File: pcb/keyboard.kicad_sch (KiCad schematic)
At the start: 6 parts

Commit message: Modified layout further
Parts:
- added SW1: SW_Push, local-library:SW_PG1350, symbol Switch:SW_Push
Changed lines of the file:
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@@
 (kicad_sch (version 20230121) (generator eeschema)
   (paper "A4")
+  (symbol (lib_id "Switch:SW_Push") (at 59.69 83.82 0) (unit 1)
+    (in_bom yes) (on_board yes) (dnp no) (fields_autoplaced)
+    (property "Reference" "SW1" (at 59.69 77.47 0)
+      (effects (font (size 1.27 1.27)))
+    )
+    (property "Value" "SW_Push" (at 59.69 80.01 0)
+      (effects (font (size 1.27 1.27)))
+    )
+    (property "Footprint" "local-library:SW_PG1350" (at 59.69 78.74 0)
+      (effects (font (size 1.27 1.27)) hide)
+    )
+    (property "Datasheet" "~" (at 59.69 78.74 0)
+      (effects (font (size 1.27 1.27)) hide)
+    )
+    (pin "1")
+    (pin "2")
+    (instances
+      (project "keyboard"
+        (path "/fc529d87-72d0-4c92-b352-ddcf4c6f7199"
+          (reference "SW1") (unit 1)
+        )
+      )
+    )
+  )
   (symbol (lib_id "Mechanical:MountingHole") (at 20.32 119.38 0) (unit 1)
     (in_bom yes) (on_board yes) (dnp no) (fields_autoplaced)

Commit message: Working on schematic and PCB
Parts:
- removed SW1: SW_Push, local-library:SW_PG1350, symbol Switch:SW_Push
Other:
- added sheet connectors (connectors.kicad_sch)
- added sheet inputs (inputs.kicad_sch)
- added sheet power (power.kicad_sch)
- added sheet stm32 (stm32.kicad_sch)
- moved on the sheet: H1, H2, H3, H4, H5, H6
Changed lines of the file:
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@@
 (kicad_sch (version 20230121) (generator eeschema)
   (paper "A4")
-  (symbol (lib_id "Switch:SW_Push") (at 59.69 83.82 0) (unit 1)
+  (symbol (lib_id "Mechanical:MountingHole") (at 40.64 143.51 0) (unit 1)
     (in_bom yes) (on_board yes) (dnp no) (fields_autoplaced)
-    (property "Reference" "SW1" (at 59.69 77.47 0)
-      (effects (font (size 1.27 1.27)))
+    (property "Reference" "H1" (at 43.18 142.875 0)
+      (effects (font (size 1.27 1.27)) (justify left))
     )
-    (property "Value" "SW_Push" (at 59.69 80.01 0)
-      (effects (font (size 1.27 1.27)))
+    (property "Value" "MountingHole" (at 43.18 145.415 0)
+      (effects (font (size 1.27 1.27)) (justify left))
     )
-    (property "Footprint" "local-library:SW_PG1350" (at 59.69 78.74 0)
+    (property "Footprint" "MountingHole:MountingHole_3.2mm_M3" (at 40.64 143.51 0)
       (effects (font (size 1.27 1.27)) hide)
     )
-    (property "Datasheet" "~" (at 59.69 78.74 0)
-      (effects (font (size 1.27 1.27)) hide)
-    )
-    (pin "1")
-    (pin "2")
-    (instances
-      (project "keyboard"
-        (path "/fc529d87-72d0-4c92-b352-ddcf4c6f7199"
-          (reference "SW1") (unit 1)
-        )
-      )
-    )
-  )
-  (symbol (lib_id "Mechanical:MountingHole") (at 20.32 119.38 0) (unit 1)
-    (in_bom yes) (on_board yes) (dnp no) (fields_autoplaced)
-    (property "Reference" "H1" (at 22.86 118.745 0)
-      (effects (font (size 1.27 1.27)) (justify left))
-    )
-    (property "Value" "MountingHole" (at 22.86 121.285 0)
-      (effects (font (size 1.27 1.27)) (justify left))
-    )
-    (property "Footprint" "MountingHole:MountingHole_3.2mm_M3" (at 20.32 119.38 0)
-      (effects (font (size 1.27 1.27)) hide)
-    )
-    (property "Datasheet" "~" (at 20.32 119.38 0)
+    (property "Datasheet" "~" (at 40.64 143.51 0)
       (effects (font (size 1.27 1.27)) hide)
     )
@@
     )
   )
-  (symbol (lib_id "Mechanical:MountingHole") (at 20.32 129.54 0) (unit 1)
+  (symbol (lib_id "Mechanical:MountingHole") (at 60.96 143.51 0) (unit 1)
     (in_bom yes) (on_board yes) (dnp no) (fields_autoplaced)
-    (property "Reference" "H3" (at 22.86 128.905 0)
+    (property "Reference" "H3" (at 63.5 142.875 0)
       (effects (font (size 1.27 1.27)) (justify left))
     )
-    (property "Value" "MountingHole" (at 22.86 131.445 0)
+    (property "Value" "MountingHole" (at 63.5 145.415 0)
       (effects (font (size 1.27 1.27)) (justify left))
     )
-    (property "Footprint" "MountingHole:MountingHole_3.2mm_M3" (at 20.32 129.54 0)
+    (property "Footprint" "MountingHole:MountingHole_3.2mm_M3" (at 60.96 143.51 0)
       (effects (font (size 1.27 1.27)) hide)
     )
-    (property "Datasheet" "~" (at 20.32 129.54 0)
+    (property "Datasheet" "~" (at 60.96 143.51 0)
       (effects (font (size 1.27 1.27)) hide)
     )
@@
     )
   )
-  (symbol (lib_id "Mechanical:MountingHole") (at 20.32 134.62 0) (unit 1)
+  (symbol (lib_id "Mechanical:MountingHole") (at 60.96 148.59 0) (unit 1)
     (in_bom yes) (on_board yes) (dnp no) (fields_autoplaced)
-    (property "Reference" "H4" (at 22.86 133.985 0)
+    (property "Reference" "H4" (at 63.5 147.955 0)
       (effects (font (size 1.27 1.27)) (justify left))
     )
-    (property "Value" "MountingHole" (at 22.86 136.525 0)
+    (property "Value" "MountingHole" (at 63.5 150.495 0)
       (effects (font (size 1.27 1.27)) (justify left))
     )
-    (property "Footprint" "MountingHole:MountingHole_3.2mm_M3" (at 20.32 134.62 0)
+    (property "Footprint" "MountingHole:MountingHole_3.2mm_M3" (at 60.96 148.59 0)
       (effects (font (size 1.27 1.27)) hide)
     )
-    (property "Datasheet" "~" (at 20.32 134.62 0)
+    (property "Datasheet" "~" (at 60.96 148.59 0)
       (effects (font (size 1.27 1.27)) hide)
     )
@@
     )
   )
-  (symbol (lib_id "Mechanical:MountingHole") (at 20.32 139.7 0) (unit 1)
+  (symbol (lib_id "Mechanical:MountingHole") (at 81.28 143.51 0) (unit 1)
     (in_bom yes) (on_board yes) (dnp no) (fields_autoplaced)
-    (property "Reference" "H5" (at 22.86 139.065 0)
+    (property "Reference" "H5" (at 83.82 142.875 0)
       (effects (font (size 1.27 1.27)) (justify left))
     )
-    (property "Value" "MountingHole" (at 22.86 141.605 0)
+    (property "Value" "MountingHole" (at 83.82 145.415 0)
       (effects (font (size 1.27 1.27)) (justify left))
     )
-    (property "Footprint" "MountingHole:MountingHole_3.2mm_M3" (at 20.32 139.7 0)
+    (property "Footprint" "MountingHole:MountingHole_3.2mm_M3" (at 81.28 143.51 0)
       (effects (font (size 1.27 1.27)) hide)
     )
-    (property "Datasheet" "~" (at 20.32 139.7 0)
+    (property "Datasheet" "~" (at 81.28 143.51 0)
       (effects (font (size 1.27 1.27)) hide)
     )
@@
     )
   )
-  (symbol (lib_id "Mechanical:MountingHole") (at 20.32 144.78 0) (unit 1)
+  (symbol (lib_id "Mechanical:MountingHole") (at 81.28 148.59 0) (unit 1)
     (in_bom yes) (on_board yes) (dnp no) (fields_autoplaced)
-    (property "Reference" "H6" (at 22.86 144.145 0)
+    (property "Reference" "H6" (at 83.82 147.955 0)
       (effects (font (size 1.27 1.27)) (justify left))
     )
-    (property "Value" "MountingHole" (at 22.86 146.685 0)
+    (property "Value" "MountingHole" (at 83.82 150.495 0)
       (effects (font (size 1.27 1.27)) (justify left))
     )
-    (property "Footprint" "MountingHole:MountingHole_3.2mm_M3" (at 20.32 144.78 0)
+    (property "Footprint" "MountingHole:MountingHole_3.2mm_M3" (at 81.28 148.59 0)
       (effects (font (size 1.27 1.27)) hide)
     )
-    (property "Datasheet" "~" (at 20.32 144.78 0)
+    (property "Datasheet" "~" (at 81.28 148.59 0)
       (effects (font (size 1.27 1.27)) hide)
     )
@@
     )
   )
-  (symbol (lib_id "Mechanical:MountingHole") (at 20.32 124.46 0) (unit 1)
+  (symbol (lib_id "Mechanical:MountingHole") (at 40.64 148.59 0) (unit 1)
     (in_bom yes) (on_board yes) (dnp no) (fields_autoplaced)
-    (property "Reference" "H2" (at 22.86 123.825 0)
+    (property "Reference" "H2" (at 43.18 147.955 0)
       (effects (font (size 1.27 1.27)) (justify left))
     )
-    (property "Value" "MountingHole" (at 22.86 126.365 0)
+    (property "Value" "MountingHole" (at 43.18 150.495 0)
       (effects (font (size 1.27 1.27)) (justify left))
     )
-    (property "Footprint" "MountingHole:MountingHole_3.2mm_M3" (at 20.32 124.46 0)
+    (property "Footprint" "MountingHole:MountingHole_3.2mm_M3" (at 40.64 148.59 0)
       (effects (font (size 1.27 1.27)) hide)
     )
-    (property "Datasheet" "~" (at 20.32 124.46 0)
+    (property "Datasheet" "~" (at 40.64 148.59 0)
       (effects (font (size 1.27 1.27)) hide)
     )
@@
       )
     )
+  )
+  (sheet (at 38.1 88.9) (size 50.8 38.1) (fields_autoplaced)
+    (stroke (width 0.1524) (type solid))
+    (fill (color 0 0 0 0.0000))
+    (property "Sheetname" "inputs" (at 38.1 88.1884 0)
+      (effects (font (size 1.27 1.27)) (justify left bottom))
+    )
+    (property "Sheetfile" "inputs.kicad_sch" (at 38.1 127.5846 0)
+      (effects (font (size 1.27 1.27)) (justify left top))
+    )
+    (instances
+      (project "keyboard"
+        (path "/fc529d87-72d0-4c92-b352-ddcf4c6f7199" (page "4"))
+      )
+    )
+  )
+  (sheet (at 38.1 38.1) (size 50.8 38.1) (fields_autoplaced)
+    (stroke (width 0.1524) (type solid))
+    (fill (color 0 0 0 0.0000))
+    (property "Sheetname" "power" (at 38.1 37.3884 0)
+      (effects (font (size 1.27 1.27)) (justify left bottom))
+    )
+    (property "Sheetfile" "power.kicad_sch" (at 38.1 76.7846 0)
+      (effects (font (size 1.27 1.27)) (justify left top))
+    )
+    (instances
+      (project "keyboard"
+        (path "/fc529d87-72d0-4c92-b352-ddcf4c6f7199" (page "2"))
+      )
+    )
+  )
+  (sheet (at 101.6 88.9) (size 50.8 38.1) (fields_autoplaced)
+    (stroke (width 0.1524) (type solid))
+    (fill (color 0 0 0 0.0000))
+    (property "Sheetname" "stm32" (at 101.6 88.1884 0)
+      (effects (font (size 1.27 1.27)) (justify left bottom))
+    )
+    (property "Sheetfile" "stm32.kicad_sch" (at 101.6 127.5846 0)
+      (effects (font (size 1.27 1.27)) (justify left top))
+    )
+    (property "Field2" "" (at 101.6 88.9 0)
+      (effects (font (size 1.27 1.27)) hide)
+    )
+    (instances
+      (project "keyboard"
+        (path "/fc529d87-72d0-4c92-b352-ddcf4c6f7199" (page "5"))
+      )
+    )
+  )
+  (sheet (at 101.6 38.1) (size 50.8 38.1) (fields_autoplaced)
+    (stroke (width 0.1524) (type solid))
+    (fill (color 0 0 0 0.0000))
+    (property "Sheetname" "connectors" (at 101.6 37.3884 0)
+      (effects (font (size 1.27 1.27)) (justify left bottom))
+    )
+    (property "Sheetfile" "connectors.kicad_sch" (at 101.6 76.7846 0)
+      (effects (font (size 1.27 1.27)) (justify left top))
+    )
+    (property "Field2" "" (at 101.6 38.1 0)
+      (effects (font (size 1.27 1.27)) hide)
+    )
+    (instances
+      (project "keyboard"
+        (path "/fc529d87-72d0-4c92-b352-ddcf4c6f7199" (page "3"))
+      )
+    )

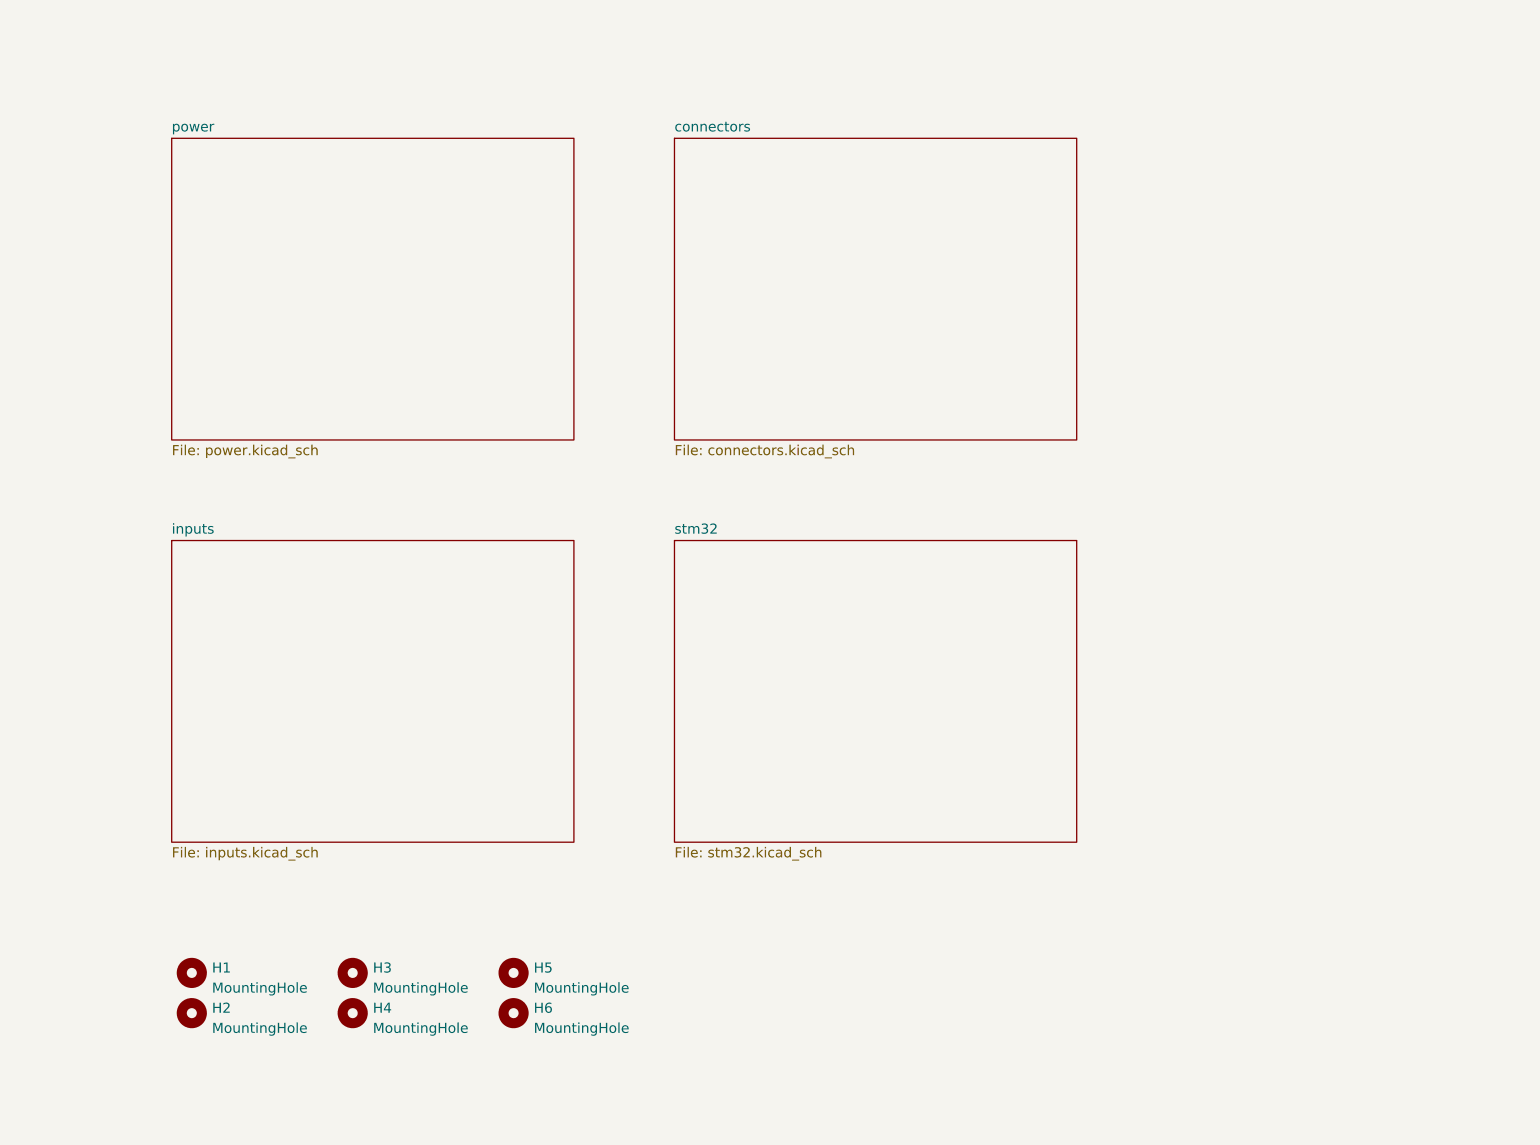
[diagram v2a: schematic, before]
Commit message: Finished off schematic
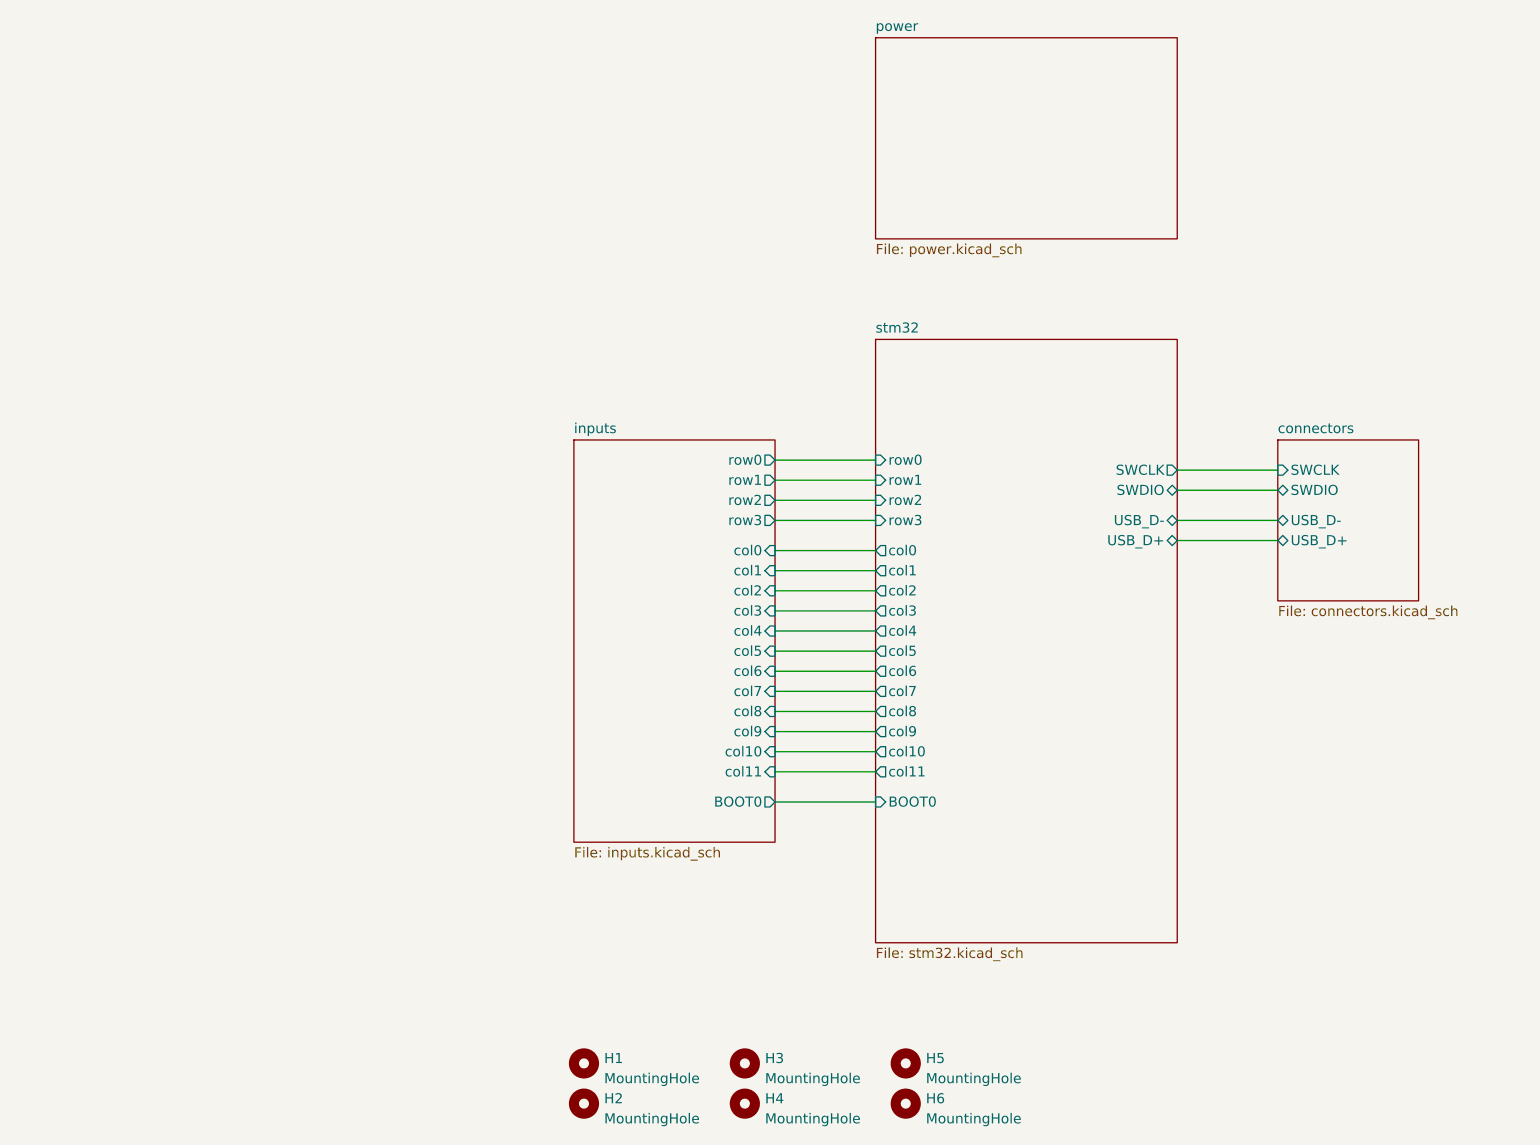
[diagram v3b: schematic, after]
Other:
- sheet connectors ports: added SWCLK, SWDIO, USB_D+, USB_D-; removed none
- sheet inputs ports: added BOOT0, col0, col1, col10, col11, col2, col3, col4, col5, col6, col7, col8, col9, row0, row1, row2, row3; removed none
- sheet stm32 ports: added BOOT0, SWCLK, SWDIO, USB_D+, USB_D-, col0, col1, col10, col11, col2, col3, col4, col5, col6, col7, col8, col9, row0, row1, row2, row3; removed none
- moved on the sheet: H1, H2, H3, H4, H5, H6

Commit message: Finished routing, ready for checks
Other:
- sheet inputs ports: added NRST; removed none
- sheet stm32 ports: added NRST; removed none
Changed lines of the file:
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@@
+    (stroke (width 0) (type default))
+  )
+  (wire (pts (xy 114.3 124.46) (xy 127 124.46))
     (stroke (width 0) (type default))
   )
@@
       (effects (font (size 1.27 1.27)) (justify right))
     )
+    (pin "NRST" output (at 114.3 124.46 0)
+      (effects (font (size 1.27 1.27)) (justify right))
+    )
     (instances
       (project "keyboard"
@@
       (effects (font (size 1.27 1.27)) (justify left))
     )
+    (pin "NRST" input (at 127 124.46 180)
+      (effects (font (size 1.27 1.27)) (justify left))
+    )
